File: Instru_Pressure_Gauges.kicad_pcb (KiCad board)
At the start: 2 copper layers, 101.6 x 53.3 mm, 35 parts, among them J1 Conn_01x08_Male, J3 647676-3, J5 Conn_01x04_Female, J6 Conn_01x04_Female, J7 Conn_01x04_Female, J8 Conn_01x03_Socket

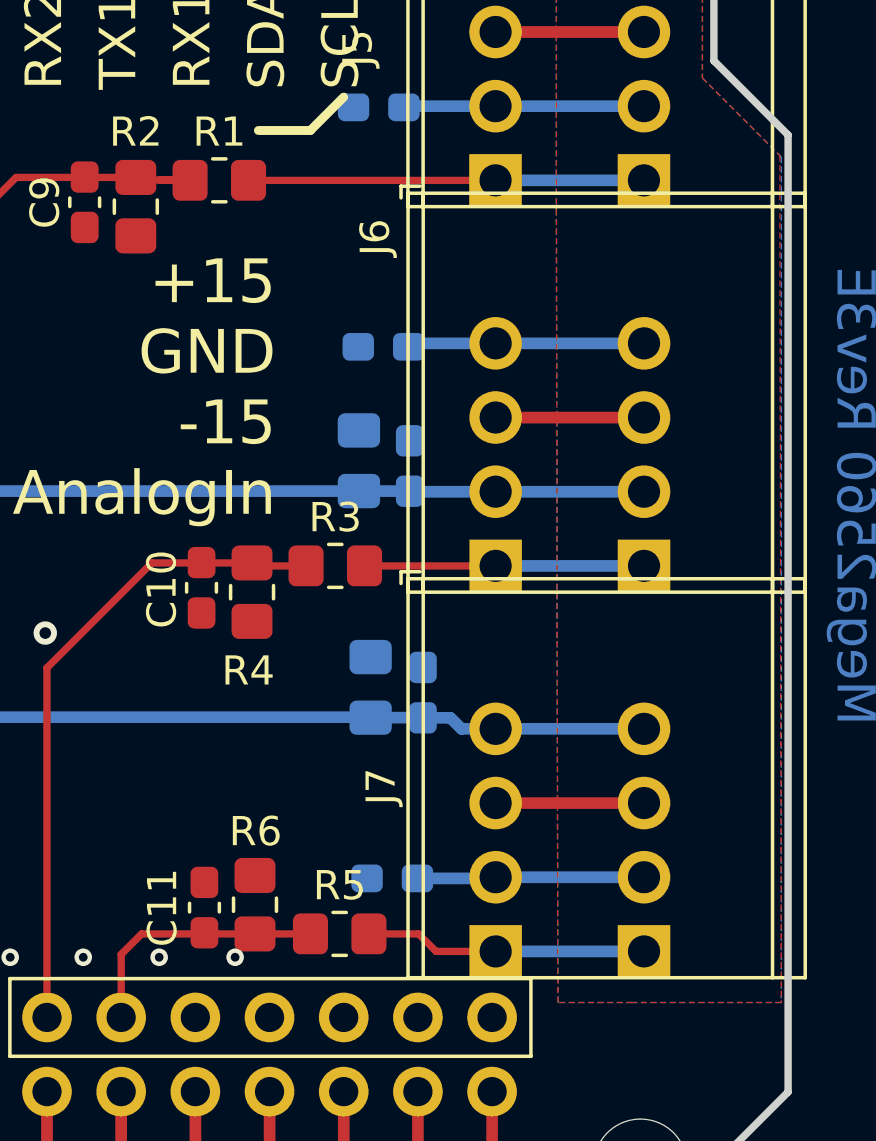
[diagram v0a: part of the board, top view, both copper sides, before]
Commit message: Corrected routing non connection
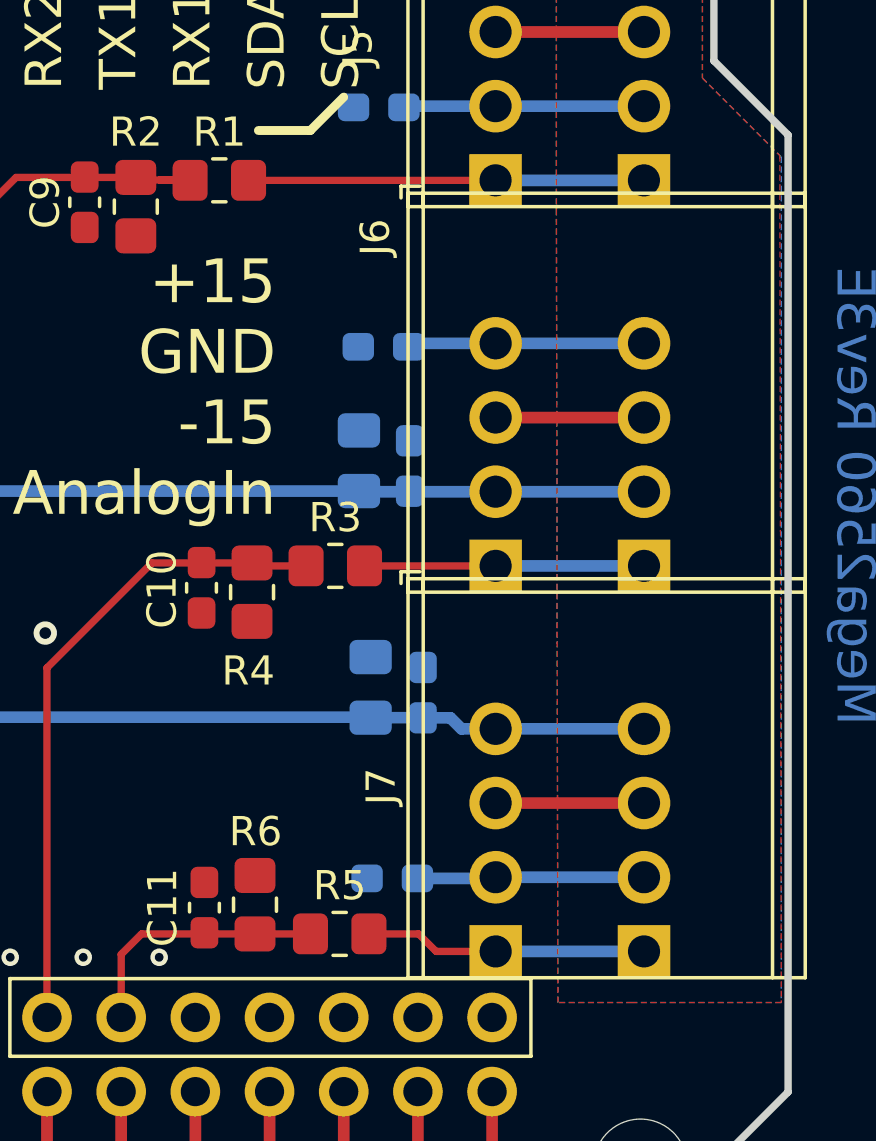
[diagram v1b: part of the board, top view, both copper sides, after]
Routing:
- net GND: vias 11 -> 10
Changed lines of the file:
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@@
       (rotate (xyz 0 0 0))
     )
-    (model ":PERSO:3D/Arduino/Mega/MEGA2560_Rev3e_in.wrl"
+    (model ":PERSO:3D/Arduino/Mega/MEGA2560_Rev3e_in.wrl" hide
       (offset (xyz 126.5 125.75 -16.5))
       (scale (xyz 1 1 1))
@@
     )
     (model ":PERSO:3D/Connectors/Header/Socket/SSQ-108-04-G-S.stp"
-      (offset (xyz -2.54 -8.89 0))
+      (offset (xyz -2.54 -8.89 -2))
       (scale (xyz 1 1 1))
-      (rotate (xyz -90 0 90))
+      (rotate (xyz 90 0 90))
     )
   )
@@
   (segment (start 178.618614 81.179907) (end 183.698614 81.179907) (width 0.4) (layer "F.Cu") (net 33))
   (segment (start 113.476 71.74) (end 113.476 74.28) (width 0.4) (layer "F.Cu") (net 33))
-  (via (at 169.701507 112.859907) (size 0.6) (drill 0.3) (layers "F.Cu" "B.Cu") (free) (net 33))
   (via (at 113.201507 101.759907) (size 0.8) (drill 0.4) (layers "F.Cu" "B.Cu") (free) (net 33))
   (via (at 133.201507 101.759907) (size 0.8) (drill 0.4) (layers "F.Cu" "B.Cu") (free) (net 33))
@@
   (segment (start 103.4508 96.7192) (end 93.526507 96.7192) (width 0.4) (layer "B.Cu") (net 54))
   (segment (start 106.311507 99.579907) (end 103.4508 96.7192) (width 0.4) (layer "B.Cu") (net 54))
-  (segment (start 175.681507 96.719407) (end 175.882007 96.919907) (width 0.4) (layer "B.Cu") (net 54))
+  (segment (start 173.941507 96.897407) (end 173.964007 96.919907) (width 0.4) (layer "B.Cu") (net 54))
+  (segment (start 173.964007 96.919907) (end 183.701507 96.919907) (width 0.4) (layer "B.Cu") (net 54))
   (segment (start 178.621507 110.119907) (end 183.701507 110.119907) (width 0.4) (layer "B.Cu") (net 54))
   (segment (start 159.864007 96.897407) (end 157.181507 99.579907) (width 0.4) (layer "B.Cu") (net 54))
   (segment (start 178.618614 83.719907) (end 175.521114 83.719907) (width 0.4) (layer "B.Cu") (net 54))
-  (segment (start 175.6813 96.7192) (end 175.681507 96.719407) (width 0.4) (layer "B.Cu") (net 54))
   (segment (start 183.698614 83.719907) (end 178.618614 83.719907) (width 0.4) (layer "B.Cu") (net 54))
-  (segment (start 173.941507 96.897407) (end 175.677007 96.897407) (width 0.4) (layer "B.Cu") (net 54))
   (segment (start 173.941507 96.897407) (end 159.864007 96.897407) (width 0.4) (layer "B.Cu") (net 54))
-  (segment (start 183.701507 96.919907) (end 178.621507 96.919907) (width 0.4) (layer "B.Cu") (net 54))
   (segment (start 175.531114 83.709907) (end 175.481114 83.759907) (width 0.4) (layer "B.Cu") (net 54))
-  (segment (start 175.882007 96.919907) (end 178.621507 96.919907) (width 0.4) (layer "B.Cu") (net 54))
   (segment (start 157.181507 99.579907) (end 106.311507 99.579907) (width 0.4) (layer "B.Cu") (net 54))
-  (segment (start 175.677007 96.897407) (end 175.681507 96.901907) (width 0.4) (layer "B.Cu") (net 54))
   (segment (start 183.698614 78.639907) (end 178.618614 78.639907) (width 0.4) (layer "B.Cu") (net 55))
   (segment (start 178.621507 91.839907) (end 183.701507 91.839907) (width 0.4) (layer "B.Cu") (net 55))
@@
   (segment (start 178.618614 78.639907) (end 175.601114 78.639907) (width 0.4) (layer "B.Cu") (net 55))
   (segment (start 175.764007 91.839907) (end 175.644007 91.959907) (width 0.4) (layer "B.Cu") (net 55))
-  (segment (start 170.161507 86.259907) (end 178.701507 86.259907) (width 0.25) (layer "F.Cu") (net 56))
-  (segment (start 170.161507 86.259907) (end 170.211507 86.209907) (width 0.25) (layer "F.Cu") (net 56))
+  (segment (start 170.161507 86.259907) (end 178.618614 86.259907) (width 0.25) (layer "F.Cu") (net 56))
   (segment (start 183.698614 86.259907) (end 178.618614 86.259907) (width 0.4) (layer "B.Cu") (net 56))
-  (segment (start 174.131507 99.459907) (end 174.181507 99.409907) (width 0.25) (layer "F.Cu") (net 57))
-  (segment (start 173.694007 99.459907) (end 173.744007 99.409907) (width 0.25) (layer "F.Cu") (net 57))
   (segment (start 174.131507 99.459907) (end 178.621507 99.459907) (width 0.25) (layer "F.Cu") (net 57))
   (segment (start 183.701507 99.459907) (end 178.621507 99.459907) (width 0.4) (layer "B.Cu") (net 57))

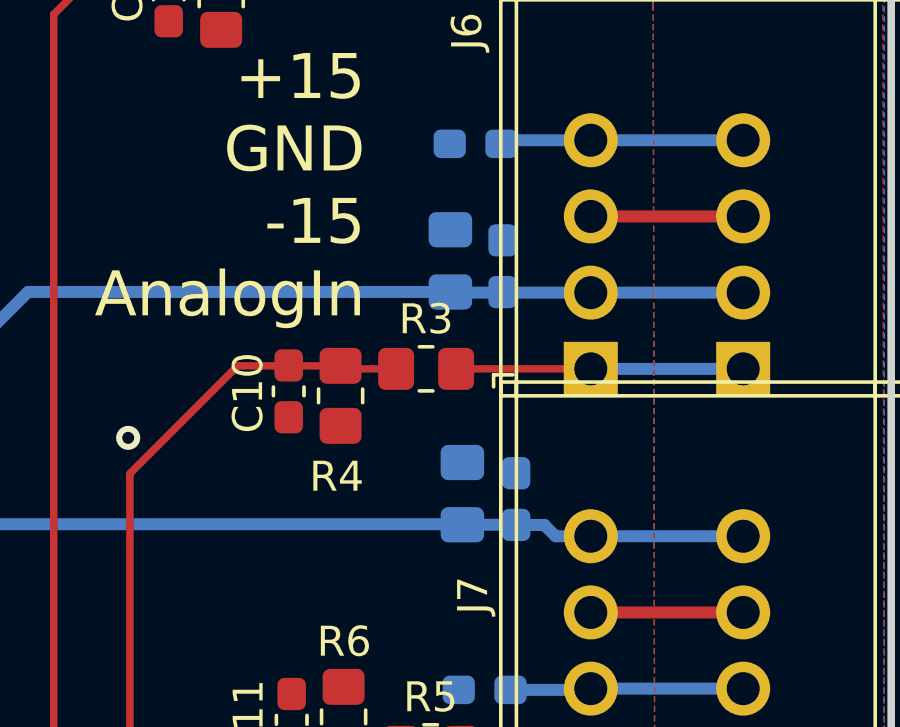
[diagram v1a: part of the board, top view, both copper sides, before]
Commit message: Update 10u for tantal
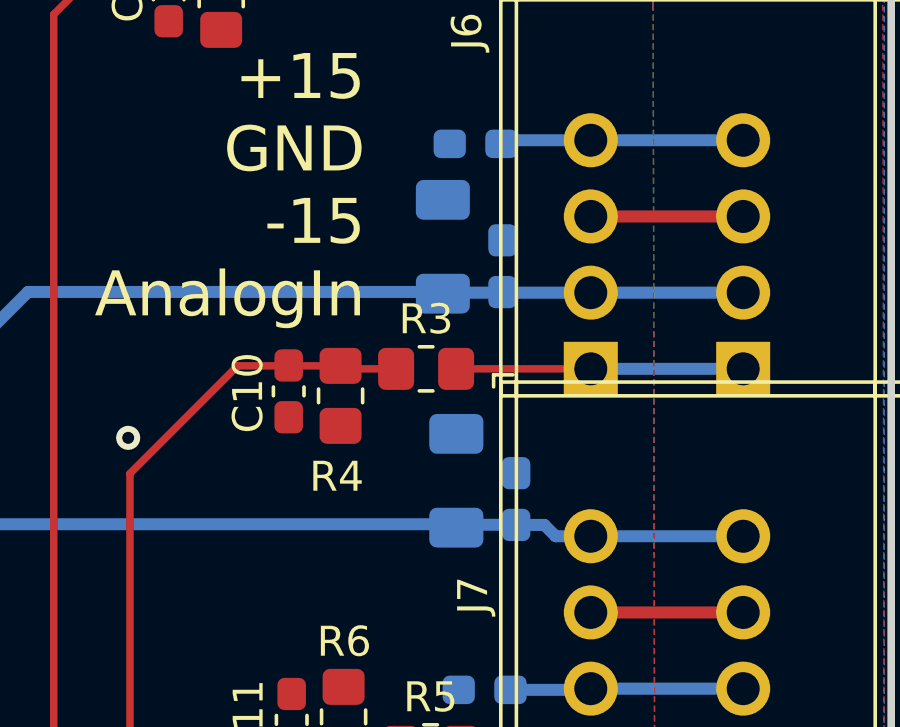
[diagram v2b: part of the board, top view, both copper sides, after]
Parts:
- C1, C3: footprint Capacitor_SMD:C_0805_2012Metric_Pad1.18x1.45mm_HandSolder -> Capacitor_SMD:C_1206_3216Metric_Pad1.33x1.80mm_HandSolder
- moved C1 0.53 mm to (173.7, 95.4)
- moved C3 0.47 mm to (174.1, 103.2)
